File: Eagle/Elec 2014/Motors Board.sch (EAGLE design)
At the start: 43 parts, among them IC1 LM18200T, IC2 LM18200T

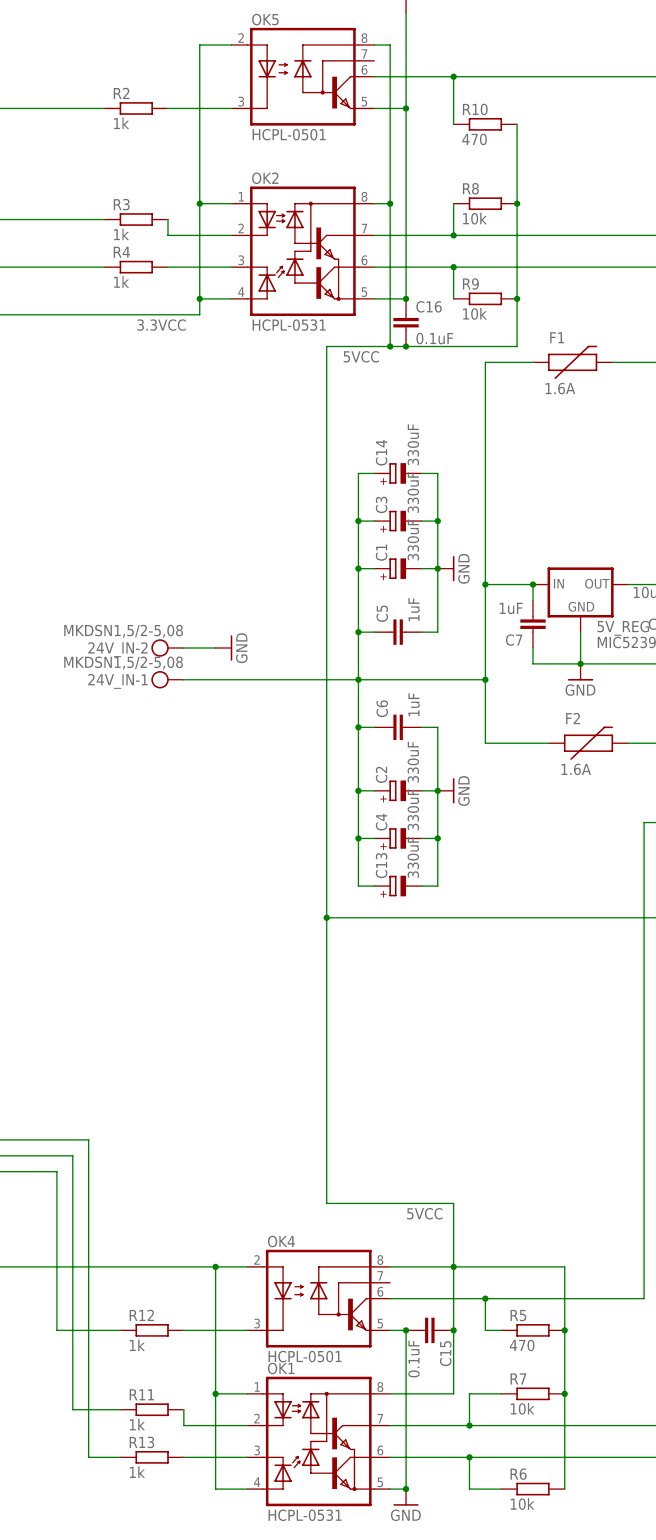
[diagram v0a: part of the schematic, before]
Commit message: Reorganise projects & cleanup
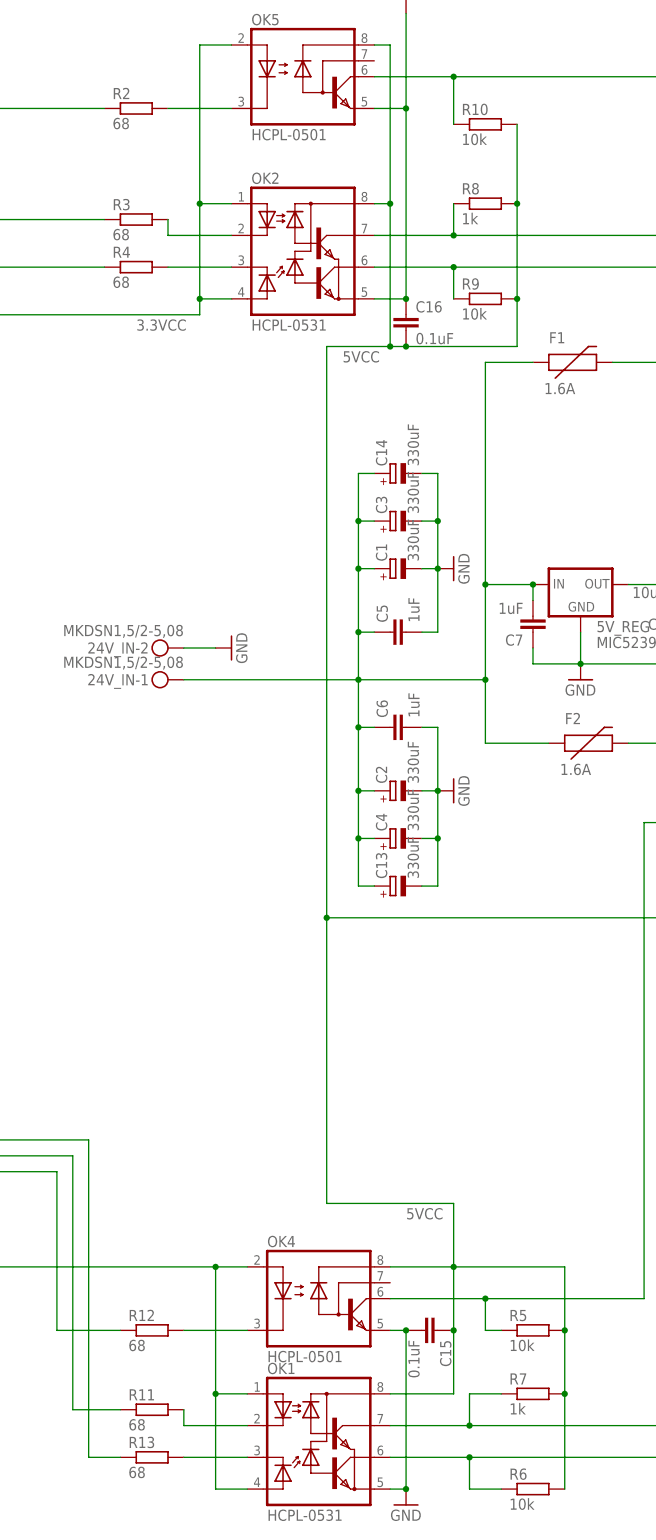
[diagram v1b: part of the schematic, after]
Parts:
- R10, R5: value 470 -> 10k
- R11, R12, R13, R2, R3, R4: value 1k -> 68
- R7, R8: value 10k -> 1k
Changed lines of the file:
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@@
 <part name="GND6" library="supply1" deviceset="GND" device=""/>
 <part name="GND1" library="supply1" deviceset="GND" device=""/>
-<part name="R2" library="rcl" deviceset="R-EU_" device="R0603" value="1k"/>
-<part name="R3" library="rcl" deviceset="R-EU_" device="R0603" value="1k"/>
-<part name="R4" library="rcl" deviceset="R-EU_" device="R0603" value="1k"/>
-<part name="R8" library="rcl" deviceset="R-EU_" device="R0603" value="10k"/>
+<part name="R2" library="rcl" deviceset="R-EU_" device="R0603" value="68"/>
+<part name="R3" library="rcl" deviceset="R-EU_" device="R0603" value="68"/>
+<part name="R4" library="rcl" deviceset="R-EU_" device="R0603" value="68"/>
+<part name="R8" library="rcl" deviceset="R-EU_" device="R0603" value="1k"/>
 <part name="R9" library="rcl" deviceset="R-EU_" device="R0603" value="10k"/>
-<part name="R10" library="rcl" deviceset="R-EU_" device="R0603" value="470"/>
+<part name="R10" library="rcl" deviceset="R-EU_" device="R0603" value="10k"/>
 <part name="GND11" library="supply1" deviceset="GND" device=""/>
 <part name="5V_REG" library="v-reg" deviceset="MIC5239" device=""/>
-<part name="R5" library="rcl" deviceset="R-EU_" device="R0603" value="470"/>
+<part name="R5" library="rcl" deviceset="R-EU_" device="R0603" value="10k"/>
 <part name="R6" library="rcl" deviceset="R-EU_" device="R0603" value="10k"/>
-<part name="R7" library="rcl" deviceset="R-EU_" device="R0603" value="10k"/>
-<part name="R11" library="rcl" deviceset="R-EU_" device="R0603" value="1k"/>
-<part name="R12" library="rcl" deviceset="R-EU_" device="R0603" value="1k"/>
-<part name="R13" library="rcl" deviceset="R-EU_" device="R0603" value="1k"/>
+<part name="R7" library="rcl" deviceset="R-EU_" device="R0603" value="1k"/>
+<part name="R11" library="rcl" deviceset="R-EU_" device="R0603" value="68"/>
+<part name="R12" library="rcl" deviceset="R-EU_" device="R0603" value="68"/>
+<part name="R13" library="rcl" deviceset="R-EU_" device="R0603" value="68"/>
 <part name="C9" library="rcl" deviceset="C-EU" device="C0603" value="10nF"/>
 <part name="C10" library="rcl" deviceset="C-EU" device="C0603" value="10nF"/>

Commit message: Small fixes after testing cards
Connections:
- net N$10 renamed DIR1_
- net N$11 renamed BREAK1_
- net N$14 renamed PWM2
- net N$15 renamed BREAK2
- net N$16 renamed DIR2
- net N$17 renamed DIR2_
- net N$18 renamed PWM2_
- net N$19 renamed BREAK2_
- net N$23 renamed DIR1
- net N$24 renamed BREAK1
- net N$25 renamed PWM1
- net N$8 renamed PWM1_
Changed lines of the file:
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@@
 </segment>
 </net>
-<net name="N$8" class="0">
+<net name="PWM1_" class="0">
 <segment>
 <pinref part="R2" gate="G$1" pin="1"/>
@@
 </segment>
 </net>
-<net name="N$10" class="0">
+<net name="DIR1_" class="0">
 <segment>
 <pinref part="R3" gate="G$1" pin="1"/>
@@
 </segment>
 </net>
-<net name="N$11" class="0">
+<net name="BREAK1_" class="0">
 <segment>
 <pinref part="R4" gate="G$1" pin="1"/>
@@
 </segment>
 </net>
-<net name="N$23" class="0">
+<net name="DIR1" class="0">
 <segment>
 <pinref part="R8" gate="G$1" pin="1"/>
@@
 </segment>
 </net>
-<net name="N$24" class="0">
+<net name="BREAK1" class="0">
 <segment>
 <wire x1="-45.72" y1="53.34" x2="-10.16" y2="53.34" width="0.1524" layer="91"/>
@@
 </segment>
 </net>
-<net name="N$25" class="0">
+<net name="PWM1" class="0">
 <segment>
 <wire x1="-45.72" y1="83.82" x2="-7.62" y2="83.82" width="0.1524" layer="91"/>
@@
 </segment>
 </net>
-<net name="N$14" class="0">
+<net name="PWM2" class="0">
 <segment>
 <wire x1="-55.88" y1="-111.76" x2="-40.64" y2="-111.76" width="0.1524" layer="91"/>
@@
 </segment>
 </net>
-<net name="N$15" class="0">
+<net name="BREAK2" class="0">
 <segment>
 <pinref part="IC2" gate="G$1" pin="BREAK"/>
@@
 </segment>
 </net>
-<net name="N$16" class="0">
+<net name="DIR2" class="0">
 <segment>
 <pinref part="R7" gate="G$1" pin="1"/>
@@
 </segment>
 </net>
-<net name="N$17" class="0">
+<net name="DIR2_" class="0">
 <segment>
 <pinref part="R11" gate="G$1" pin="1"/>
@@
 </segment>
 </net>
-<net name="N$18" class="0">
+<net name="PWM2_" class="0">
 <segment>
 <pinref part="R12" gate="G$1" pin="1"/>
@@
 </segment>
 </net>
-<net name="N$19" class="0">
+<net name="BREAK2_" class="0">
 <segment>
 <wire x1="-104.14" y1="-86.36" x2="-104.14" y2="-137.16" width="0.1524" layer="91"/>
